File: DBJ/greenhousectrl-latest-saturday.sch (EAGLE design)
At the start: 56 parts, among them IC1 ATMEGA168TQFP-08, IC4 L298, J1 POWER_JACKPTH, K2 G5LE, Q1 MMBT2222A, SW2 MOMENTARYBUTTON, U2 V_REG_317SMD, X1 CRYSTALS-NOGND-HC49

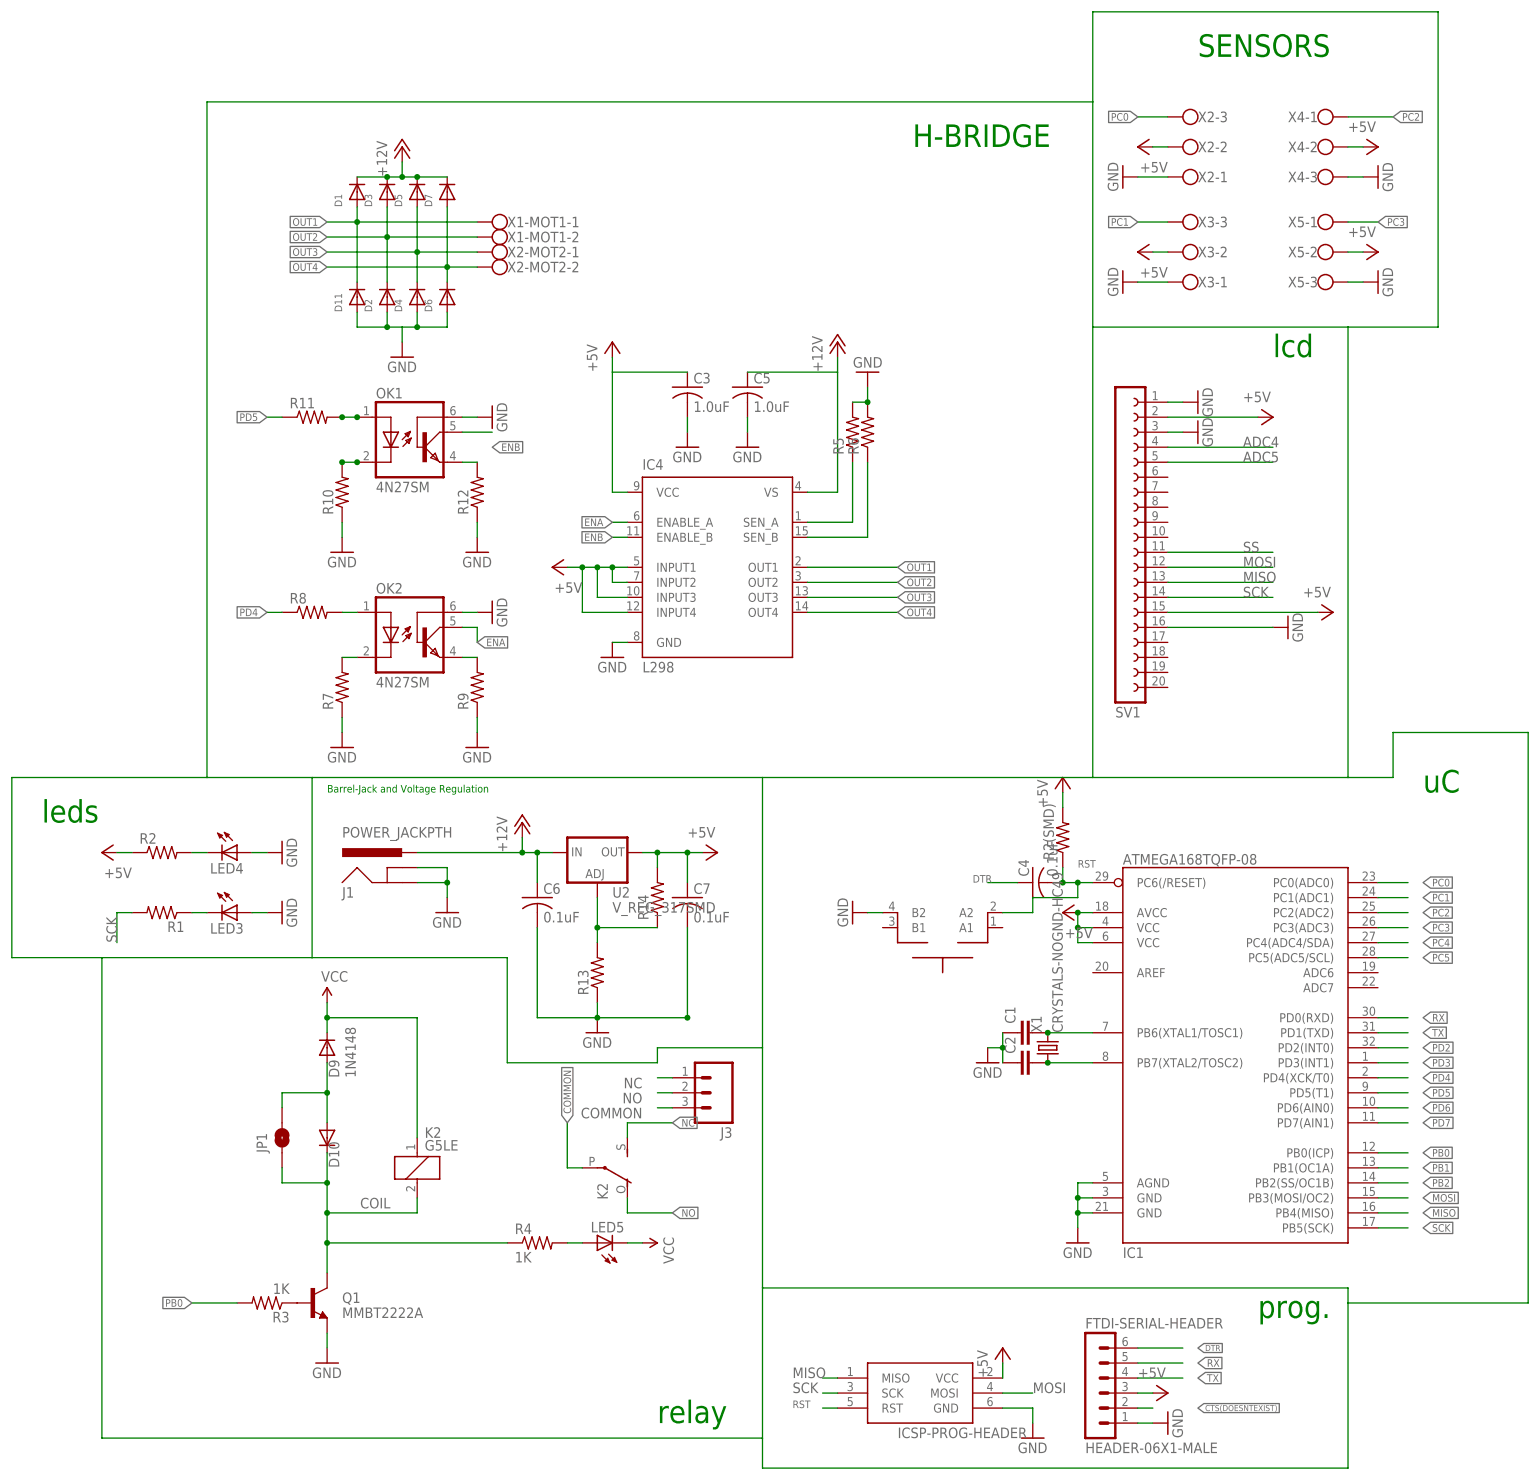
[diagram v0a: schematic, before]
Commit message: erc and new vreg
ran erc on schematic, re-organized repository, used 7824DTvreg instead
of the vreg previously used due to erc giving errors
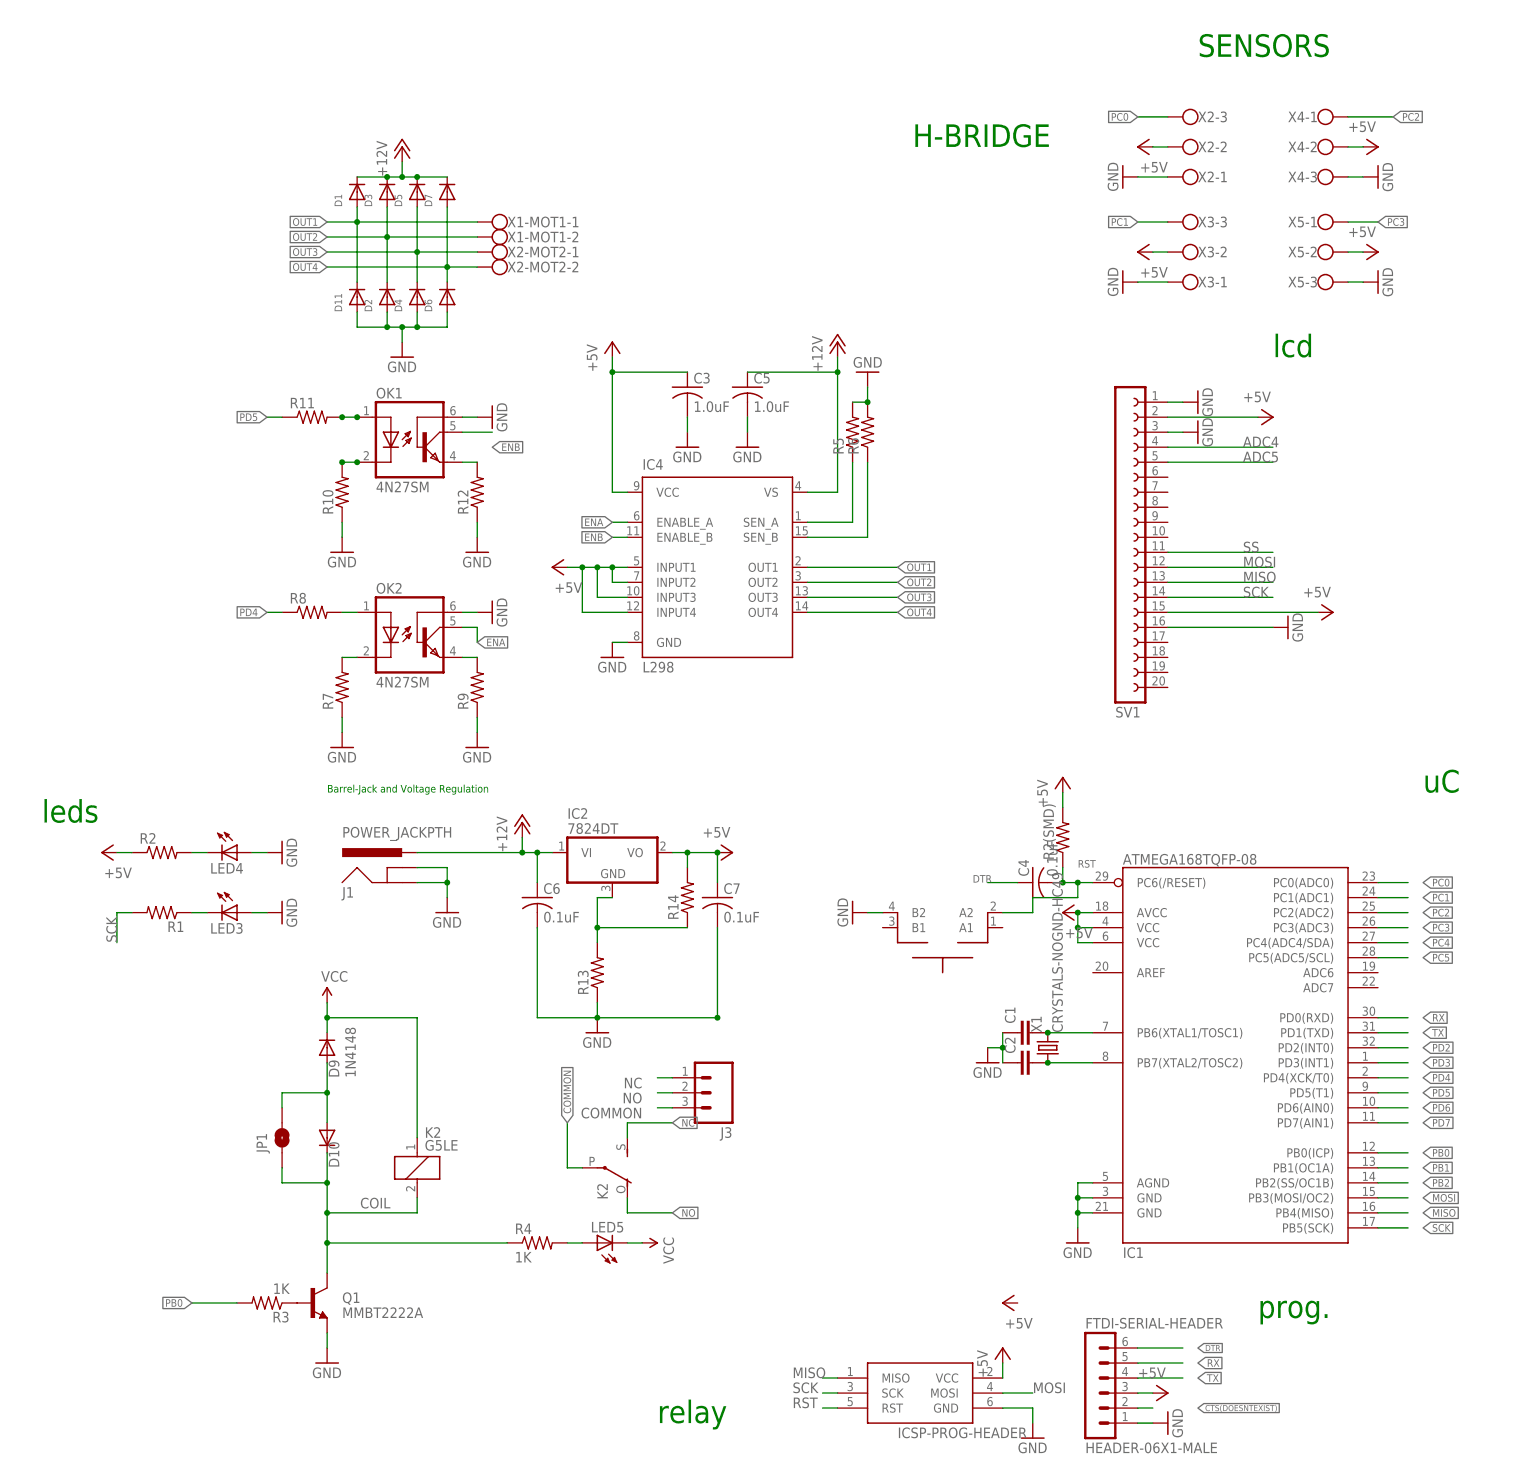
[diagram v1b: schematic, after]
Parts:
- removed U2: V_REG_317SMD, SparkFun-PowerIC:V_REG_317SMD
- added IC2: 7824DT, linear:7824DT
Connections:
- net +12V: now also IC2.VI; no longer U2.IN
- net +5V: now also IC2.VO; no longer U2.OUT
- net N$7: now also IC2.GND; no longer U2.ADJ
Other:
- moved on the sheet: C7, R14
